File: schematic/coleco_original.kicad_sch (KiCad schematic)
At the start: 6 parts

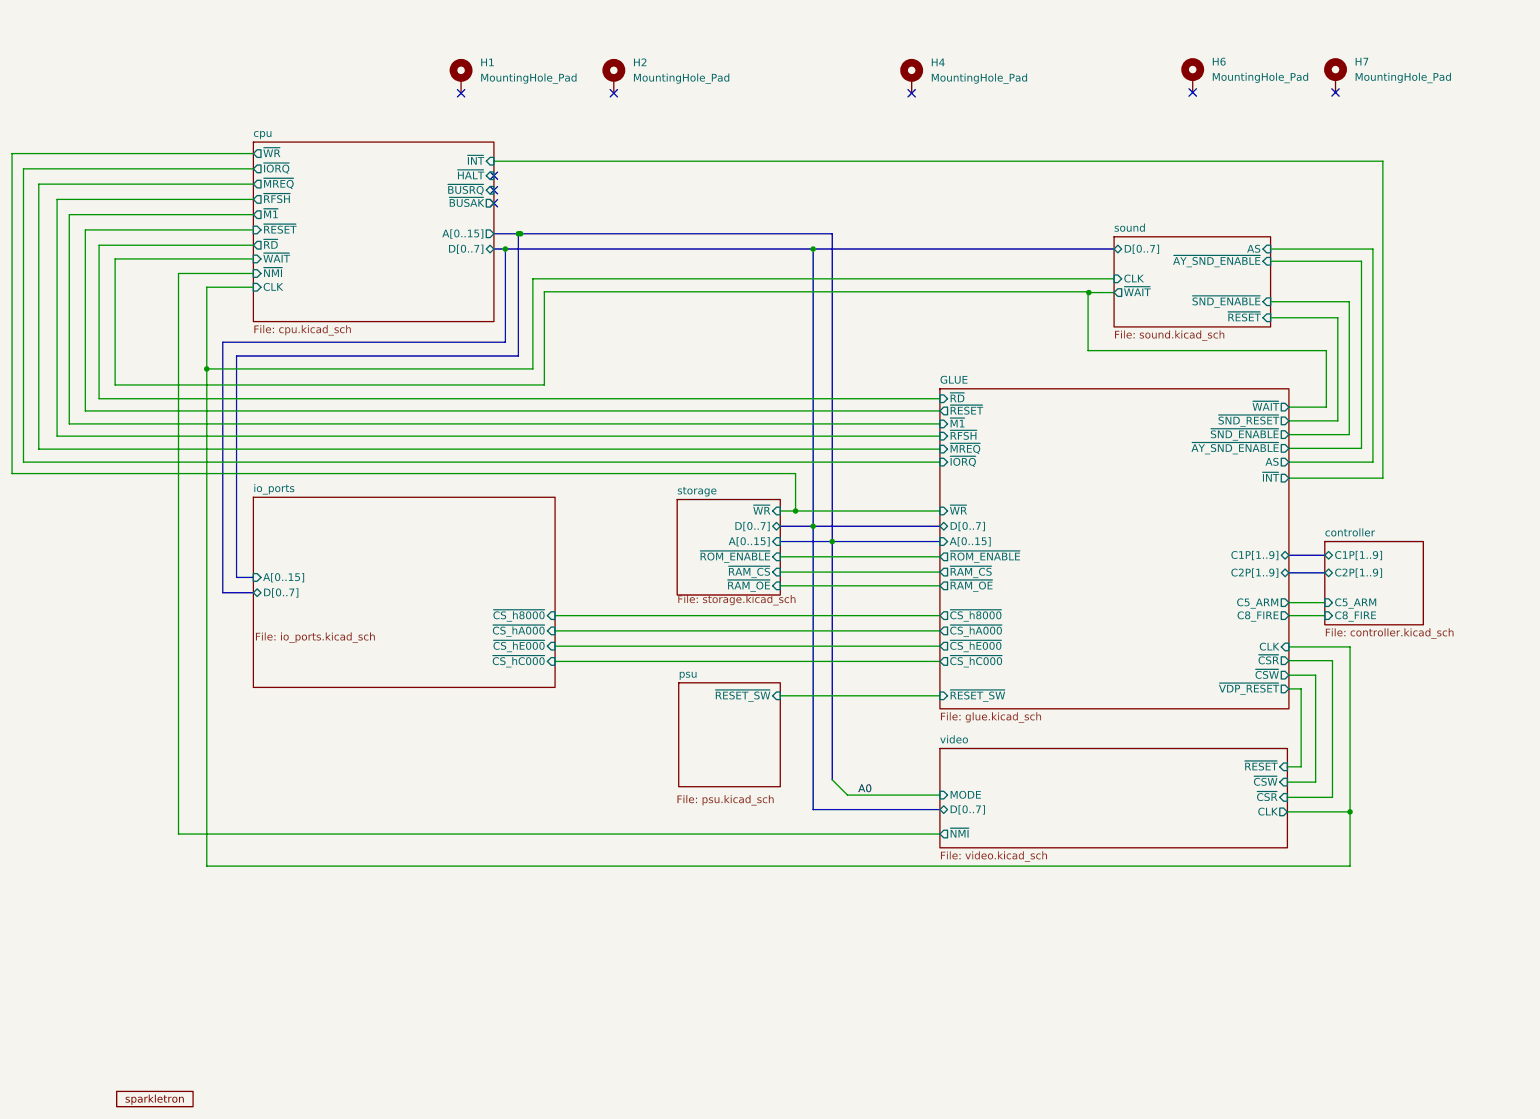
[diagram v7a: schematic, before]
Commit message: complete ram mirror when banks not enabled.
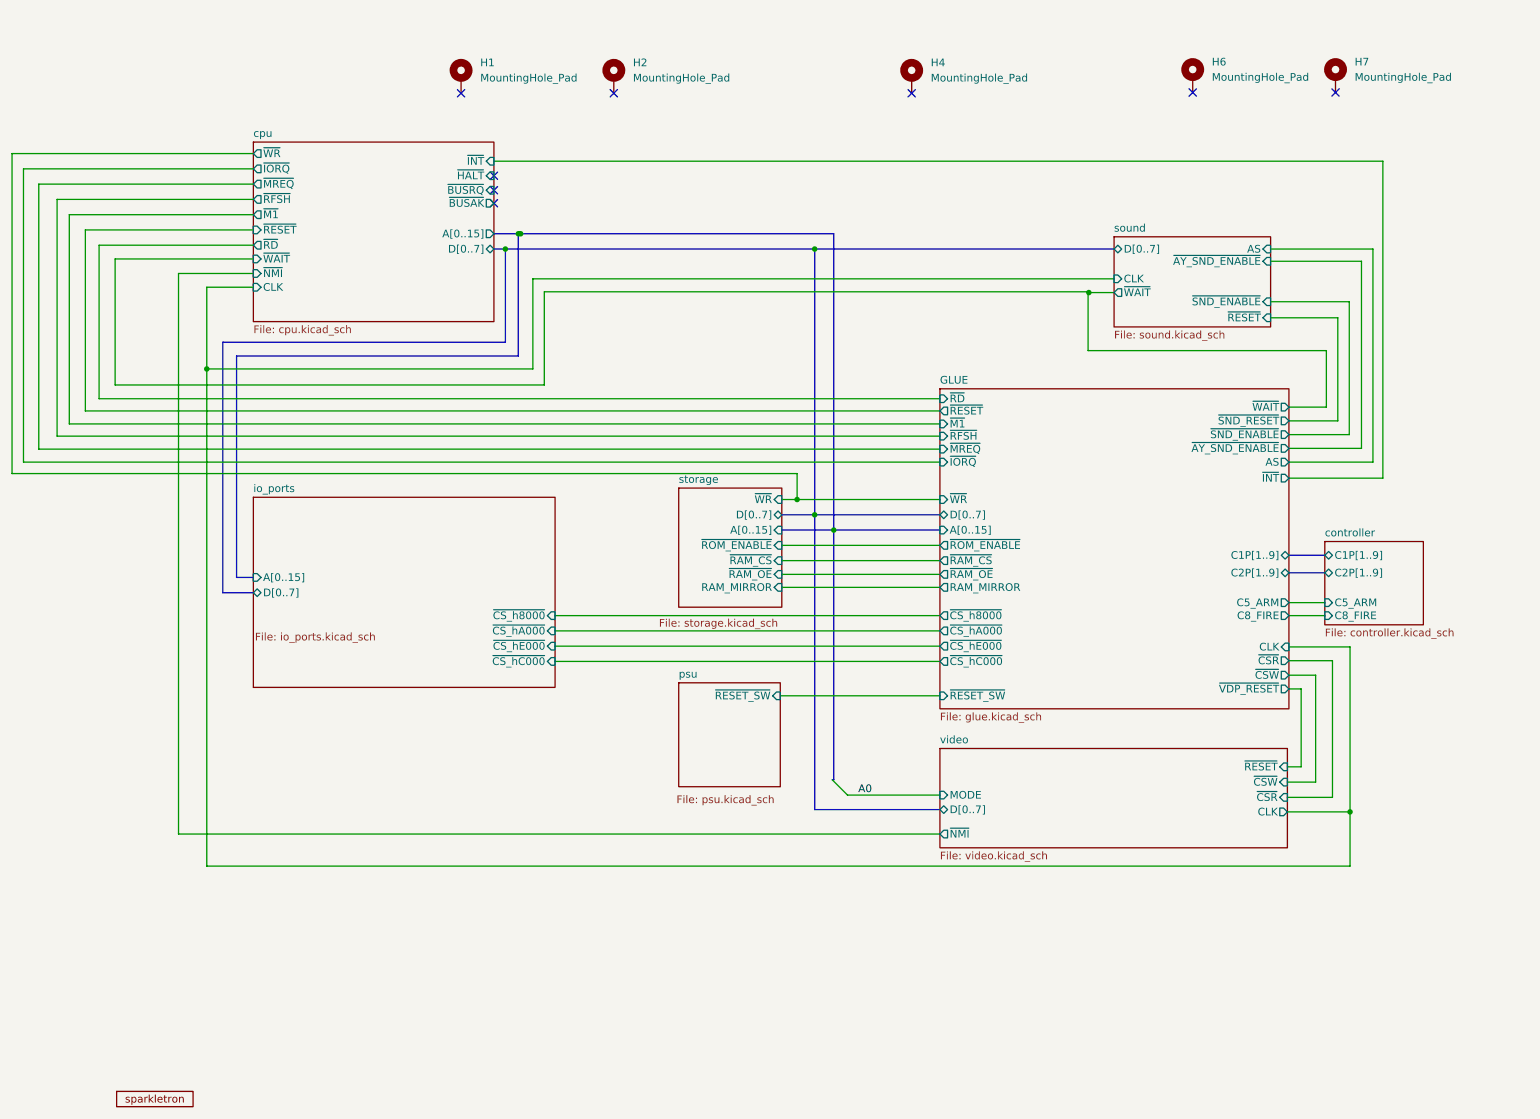
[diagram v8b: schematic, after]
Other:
- sheet GLUE ports: added RAM_MIRROR; removed none
- sheet storage ports: added RAM_MIRROR; removed none
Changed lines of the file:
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@@
   (junction (at 52.451 77.978) (diameter 0) (color 0 0 0 0)
   )
-  (junction (at 153.289 104.14) (diameter 0) (color 0 0 0 0)
-  )
-  (junction (at 156.464 106.68) (diameter 0) (color 0 0 0 0)
+  (junction (at 153.543 102.235) (diameter 0) (color 0 0 0 0)
+  )
+  (junction (at 156.718 104.775) (diameter 0) (color 0 0 0 0)
   )
   (junction (at 242.57 151.638) (diameter 0) (color 0 0 0 0)
   )
-  (junction (at 150.368 101.6) (diameter 0) (color 0 0 0 0)
+  (junction (at 150.622 99.695) (diameter 0) (color 0 0 0 0)
   )
   (junction (at 104.267 55.499) (diameter 0) (color 0 0 0 0)
@@
   (junction (at 102.108 58.039) (diameter 0) (color 0 0 0 0)
   )
+  (junction (at 153.543 58.039) (diameter 0) (color 0 0 0 0)
+  )
   (junction (at 104.648 55.499) (diameter 0) (color 0 0 0 0)
-  )
-  (junction (at 153.289 58.039) (diameter 0) (color 0 0 0 0)
   )
   (no_connect (at 216.408 32.004))
@@
     (stroke (width 0) (type default))
   )
-  (wire (pts (xy 20.066 95.377) (xy 150.368 95.377))
+  (wire (pts (xy 20.066 95.377) (xy 150.622 95.377))
     (stroke (width 0) (type default))
   )
@@
     (stroke (width 0) (type default))
   )
+  (bus (pts (xy 156.718 146.304) (xy 156.464 146.304))
+    (stroke (width 0) (type default))
+  )
   (wire (pts (xy 236.855 128.905) (xy 232.41 128.905))
     (stroke (width 0) (type default))
@@
     (stroke (width 0) (type default))
   )
-  (wire (pts (xy 147.828 111.76) (xy 174.371 111.76))
+  (wire (pts (xy 148.082 109.855) (xy 174.371 109.855))
     (stroke (width 0) (type default))
   )
@@
     (stroke (width 0) (type default))
   )
-  (bus (pts (xy 153.289 58.039) (xy 203.327 58.039))
-    (stroke (width 0) (type default))
-  )
   (wire (pts (xy 242.57 151.638) (xy 242.57 160.655))
     (stroke (width 0) (type default))
@@
     (stroke (width 0) (type default))
   )
-  (bus (pts (xy 153.289 104.14) (xy 153.289 151.257))
-    (stroke (width 0) (type default))
-  )
-  (bus (pts (xy 104.648 55.499) (xy 156.464 55.499))
+  (bus (pts (xy 153.543 102.235) (xy 153.543 151.257))
+    (stroke (width 0) (type default))
+  )
+  (bus (pts (xy 104.648 55.499) (xy 156.718 55.499))
     (stroke (width 0) (type default))
   )
@@
     (stroke (width 0) (type default))
   )
-  (bus (pts (xy 147.828 106.68) (xy 156.464 106.68))
+  (bus (pts (xy 148.082 104.775) (xy 156.718 104.775))
     (stroke (width 0) (type default))
   )
@@
     (stroke (width 0) (type default))
   )
+  (bus (pts (xy 153.543 58.039) (xy 203.327 58.039))
+    (stroke (width 0) (type default))
+  )
   (wire (pts (xy 232.41 93.472) (xy 246.38 93.472))
     (stroke (width 0) (type default))
@@
     (stroke (width 0) (type default))
   )
-  (wire (pts (xy 150.368 101.6) (xy 174.371 101.6))
-    (stroke (width 0) (type default))
-  )
-  (bus (pts (xy 102.108 58.039) (xy 153.289 58.039))
+  (wire (pts (xy 150.622 99.695) (xy 174.371 99.695))
+    (stroke (width 0) (type default))
+  )
+  (bus (pts (xy 102.108 58.039) (xy 153.543 58.039))
     (stroke (width 0) (type default))
   )
@@
     (stroke (width 0) (type default))
   )
-  (bus (pts (xy 156.464 106.68) (xy 156.464 146.304))
+  (bus (pts (xy 156.718 104.775) (xy 156.718 146.304))
     (stroke (width 0) (type default))
   )
@@
     (stroke (width 0) (type default))
   )
-  (bus (pts (xy 156.464 55.499) (xy 156.464 106.68))
+  (bus (pts (xy 156.718 55.499) (xy 156.718 104.775))
     (stroke (width 0) (type default))
   )
@@
     (stroke (width 0) (type default))
   )
-  (bus (pts (xy 156.464 106.68) (xy 174.371 106.68))
+  (bus (pts (xy 156.718 104.775) (xy 174.371 104.775))
     (stroke (width 0) (type default))
   )
@@
     (stroke (width 0) (type default))
   )
+  (wire (pts (xy 148.082 114.3) (xy 174.371 114.3))
+    (stroke (width 0) (type default))
+  )
   (bus (pts (xy 57.404 112.649) (xy 60.198 112.649))
     (stroke (width 0) (type default))
@@
     (stroke (width 0) (type default))
   )
-  (wire (pts (xy 147.828 109.22) (xy 174.371 109.22))
+  (wire (pts (xy 148.082 107.315) (xy 174.371 107.315))
     (stroke (width 0) (type default))
   )
@@
     (stroke (width 0) (type default))
   )
-  (wire (pts (xy 147.828 101.6) (xy 150.368 101.6))
+  (wire (pts (xy 148.082 99.695) (xy 150.622 99.695))
     (stroke (width 0) (type default))
   )
@@
     (stroke (width 0) (type default))
   )
-  (bus (pts (xy 147.828 104.14) (xy 153.289 104.14))
+  (bus (pts (xy 148.082 102.235) (xy 153.543 102.235))
     (stroke (width 0) (type default))
   )
@@
     (stroke (width 0) (type default))
   )
-  (bus (pts (xy 153.289 58.039) (xy 153.289 104.14))
-    (stroke (width 0) (type default))
-  )
-  (wire (pts (xy 150.368 95.377) (xy 150.368 101.6))
+  (bus (pts (xy 153.543 58.039) (xy 153.543 102.235))
+    (stroke (width 0) (type default))
+  )
+  (wire (pts (xy 150.622 95.377) (xy 150.622 99.695))
     (stroke (width 0) (type default))
   )
@@
     (stroke (width 0) (type default))
   )
-  (wire (pts (xy 147.828 114.046) (xy 174.371 114.046))
+  (wire (pts (xy 148.082 112.141) (xy 174.371 112.141))
     (stroke (width 0) (type default))
   )
@@
     (stroke (width 0) (type default))
   )
-  (bus (pts (xy 153.289 151.257) (xy 174.371 151.257))
+  (bus (pts (xy 153.543 151.257) (xy 174.371 151.257))
     (stroke (width 0) (type default))
   )
@@
     (stroke (width 0) (type default))
   )
-  (bus (pts (xy 153.289 104.14) (xy 174.371 104.14))
+  (bus (pts (xy 153.543 102.235) (xy 174.371 102.235))
     (stroke (width 0) (type default))
   )
@@
     )
   )
-  (sheet (at 130.683 99.695) (size 17.145 15.875)
+  (sheet (at 130.937 97.79) (size 17.145 19.812)
     (stroke (width 0) (type solid))
     (fill (color 0 0 0 0.0000))
-    (property "Sheetname" "storage" (at 130.683 98.9834 0)
+    (property "Sheetname" "storage" (at 130.937 97.0784 0)
       (effects (font (size 1.27 1.27)) (justify left bottom))
     )
-    (property "Sheetfile" "storage.kicad_sch" (at 130.683 115.57 0)
+    (property "Sheetfile" "storage.kicad_sch" (at 127.635 119.507 0)
       (effects (font (size 1.27 1.27)) (justify left top))
     )
-    (pin "D[0..7]" bidirectional (at 147.828 104.14 0)
-      (effects (font (size 1.27 1.27)) (justify right))
-    )
-    (pin "A[0..15]" input (at 147.828 106.68 0)
-      (effects (font (size 1.27 1.27)) (justify right))
-    )
-    (pin "~{WR}" input (at 147.828 101.6 0)
-      (effects (font (size 1.27 1.27)) (justify right))
-    )
-    (pin "~{ROM_ENABLE}" input (at 147.828 109.22 0)
-      (effects (font (size 1.27 1.27)) (justify right))
-    )
-    (pin "~{RAM_CS}" input (at 147.828 111.76 0)
-      (effects (font (size 1.27 1.27)) (justify right))
-    )
-    (pin "~{RAM_OE}" input (at 147.828 114.046 0)
+    (pin "D[0..7]" bidirectional (at 148.082 102.235 0)
+      (effects (font (size 1.27 1.27)) (justify right))
+    )
+    (pin "A[0..15]" input (at 148.082 104.775 0)
+      (effects (font (size 1.27 1.27)) (justify right))
+    )
+    (pin "~{WR}" input (at 148.082 99.695 0)
+      (effects (font (size 1.27 1.27)) (justify right))
+    )
+    (pin "~{ROM_ENABLE}" input (at 148.082 107.315 0)
+      (effects (font (size 1.27 1.27)) (justify right))
+    )
+    (pin "~{RAM_CS}" input (at 148.082 109.855 0)
+      (effects (font (size 1.27 1.27)) (justify right))
+    )
+    (pin "~{RAM_OE}" input (at 148.082 112.141 0)
+      (effects (font (size 1.27 1.27)) (justify right))
+    )
+    (pin "RAM_MIRROR" input (at 148.082 114.3 0)
       (effects (font (size 1.27 1.27)) (justify right))
     )
@@
       (effects (font (size 1.27 1.27)) (justify left top))
     )
-    (pin "~{WR}" input (at 174.371 101.6 180)
+    (pin "~{WR}" input (at 174.371 99.695 180)
       (effects (font (size 1.27 1.27)) (justify left))
     )
@@
       (effects (font (size 1.27 1.27)) (justify right))
     )
-    (pin "D[0..7]" bidirectional (at 174.371 104.14 180)
-      (effects (font (size 1.27 1.27)) (justify left))
-    )
-    (pin "A[0..15]" input (at 174.371 106.68 180)
+    (pin "D[0..7]" bidirectional (at 174.371 102.235 180)
+      (effects (font (size 1.27 1.27)) (justify left))
+    )
+    (pin "A[0..15]" input (at 174.371 104.775 180)
       (effects (font (size 1.27 1.27)) (justify left))
     )
@@
       (effects (font (size 1.27 1.27)) (justify right))
     )
-    (pin "~{ROM_ENABLE}" output (at 174.371 109.22 180)
-      (effects (font (size 1.27 1.27)) (justify left))
-    )
-    (pin "~{RAM_CS}" output (at 174.371 111.76 180)
+    (pin "~{ROM_ENABLE}" output (at 174.371 107.315 180)
+      (effects (font (size 1.27 1.27)) (justify left))
+    )
+    (pin "~{RAM_CS}" output (at 174.371 109.855 180)
       (effects (font (size 1.27 1.27)) (justify left))
     )
@@
       (effects (font (size 1.27 1.27)) (justify left))
     )
-    (pin "~{RAM_OE}" output (at 174.371 114.046 180)
+    (pin "~{RAM_OE}" output (at 174.371 112.141 180)
       (effects (font (size 1.27 1.27)) (justify left))
     )
@@
       (effects (font (size 1.27 1.27)) (justify right))
     )
-    (instances
+    (pin "RAM_MIRROR" output (at 174.371 114.3 180)
+      (effects (font (size 1.27 1.27)) (justify left))
+    )
+    (instances
